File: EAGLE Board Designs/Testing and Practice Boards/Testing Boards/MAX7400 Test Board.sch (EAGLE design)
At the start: 5 parts

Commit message: change silkscreen
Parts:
- U$1: value MAX7400 -> MAX74
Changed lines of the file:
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@@
 <drawing>
 <settings>
-<setting alwaysvectorfont="no"/>
+<setting alwaysvectorfont="yes"/>
 <setting verticaltext="up"/>
 </settings>
@@
 <part name="C3" library="HyTechDevices" deviceset="CAP" device="0603-CAP" value="0.1uF"/>
 <part name="GND4" library="HyTechSupplies" deviceset="GND" device=""/>
-<part name="U$1" library="HyTechDevices" deviceset="MAX7400" device=""/>
+<part name="U$1" library="HyTechDevices" deviceset="MAX7400" device="" value="MAX74"/>
 </parts>
 <sheets>

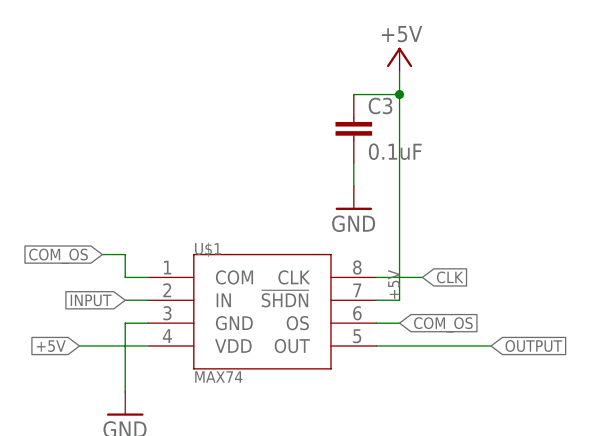
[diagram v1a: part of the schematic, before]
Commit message: Silkscreen changes
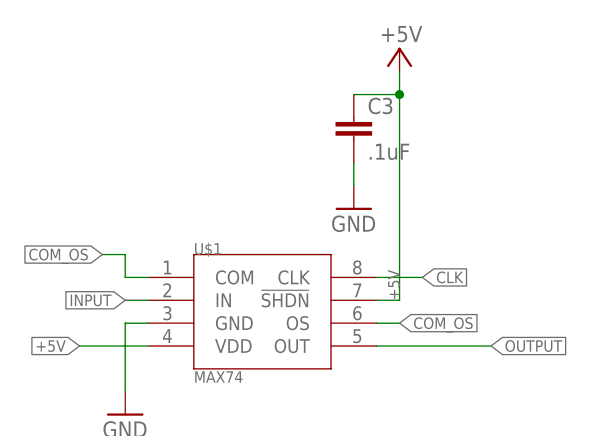
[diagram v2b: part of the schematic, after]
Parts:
- C3: value 0.1uF -> .1uF
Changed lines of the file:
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@@
 <drawing>
 <settings>
-<setting alwaysvectorfont="yes"/>
+<setting alwaysvectorfont="no"/>
 <setting verticaltext="up"/>
 </settings>
@@
 <part name="C2" library="HyTechDevices" deviceset="CAP" device="0603-CAP" value="0.1uF"/>
 <part name="GND3" library="HyTechSupplies" deviceset="GND" device=""/>
-<part name="C3" library="HyTechDevices" deviceset="CAP" device="0603-CAP" value="0.1uF"/>
+<part name="C3" library="HyTechDevices" deviceset="CAP" device="0603-CAP" value=".1uF"/>
 <part name="GND4" library="HyTechSupplies" deviceset="GND" device=""/>
 <part name="U$1" library="HyTechDevices" deviceset="MAX7400" device="" value="MAX74"/>
